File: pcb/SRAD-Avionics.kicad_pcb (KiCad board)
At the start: 4 copper layers, 75.8 x 82.9 mm, 48 parts, among them J1 Conn_01x02_Socket, J2 Conn_01x02_Socket, J3 USB_C_Receptacle_USB2.0_16P, SW1 SW_DIP_x01, U1 MS5607-02BA, U2 STM32H503RBTx, U3 MCP73831-2-MC, U4 TC2185-3.3VxCTTR, U5 USBLC6-2SC6, U6 TCAN332G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

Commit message: New dir structure. USB, CAN, power layout done. Started CubeIDE project
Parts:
- moved R4 38.6 mm to (146.3, 57.6)
- moved C2 38.3 mm to (138.3, 58.7), turned to -90 degrees
- moved C3 37.8 mm to (137.9, 66.3), turned to -90 degrees
- moved C8 36.1 mm to (157.5, 66.6), turned to 90 degrees
- moved D2 35.3 mm to (146.3, 60.7)
- moved U4 35.1 mm to (140.6, 66.6), turned to -90 degrees
- moved C4 35.1 mm to (140.5, 69.6)
- moved C9 34.0 mm to (167.9, 66.6), turned to 90 degrees
- moved R3 33.9 mm to (150.3, 57.6), turned to 180 degrees
- moved C5 33.3 mm to (143.3, 66.8), turned to 90 degrees
- moved C1 33.3 mm to (142.9, 58.7), turned to -90 degrees
- moved TP4 32.4 mm to (180.3, 62.9)
- moved R1 32.4 mm to (146.3, 63.7)
- moved C7 30.8 mm to (149.5, 80.9), turned to 180 degrees
- moved D1 30.7 mm to (150.3, 60.7)
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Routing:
- net +3.3V: track 17.0 -> 60.1 mm, vias 6 -> 17
- net GNDD: track 22.4 -> 60.9 mm, vias 12 -> 38
- net /FDCAN_TX: track 0.00 -> 33.6 mm, vias 0 -> 2
- net /FDCAN_RX: track 0.00 -> 31.7 mm, vias 0 -> 2
- net Net-(C6-Pad1): track 0.00 -> 28.7 mm, vias 0 -> 2
- net VDDA: track 0.00 -> 13.3 mm, vias 0 -> 3
- net /Battery Management/V_BAT: track 0.00 -> 13.2 mm, vias 0 -> 4
- net /Battery Management/STAT: track 0.00 -> 12.6 mm, vias 0 -> 2
- net /BOOT0: track 2.14 -> 11.7 mm
- net /Battery Management/V_USB: track 5.80 -> 12.7 mm, vias 3 -> 6
- net GNDA: track 0.00 -> 6.33 mm
- net Net-(U3-PROG): track 0.00 -> 6.32 mm
- net Net-(D2-K): track 0.00 -> 3.13 mm
- net Net-(D1-A): track 0.00 -> 3.12 mm
- net Net-(U4-BP): track 0.00 -> 1.88 mm
- added copper zone on In2.Cu, net +3.3V
- added copper zone on In2.Cu, net /Battery Management/V_BAT

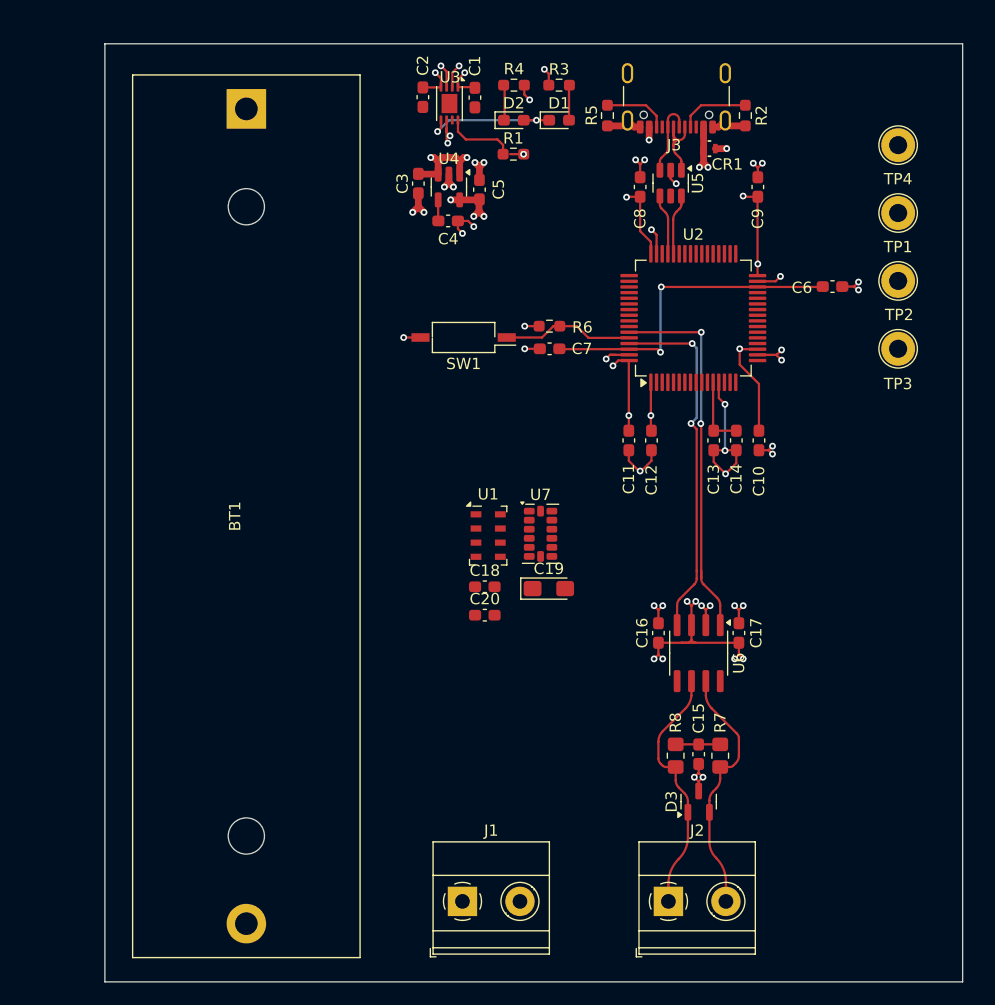
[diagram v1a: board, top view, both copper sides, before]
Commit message: Routed reset monitor, all test points, 128 MBit flash, sensors, analog-digital jumper switches
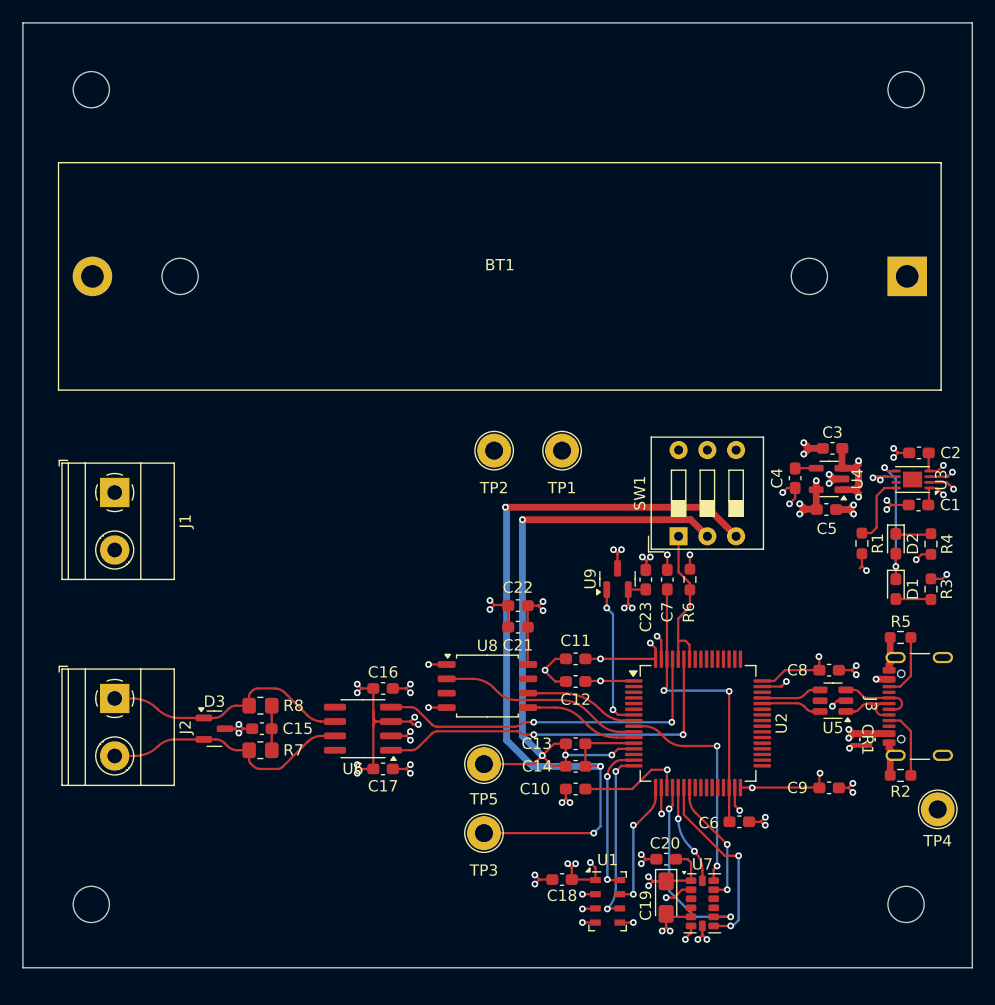
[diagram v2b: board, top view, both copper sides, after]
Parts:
- added C21: 100nF, Capacitor_SMD:C_0603_1608Metric_Pad1.08x0.95mm_HandSolder, F.Cu at (146.7, 105.5)
- added C22: 4.7uF, Capacitor_SMD:C_0603_1608Metric_Pad1.08x0.95mm_HandSolder, F.Cu at (146.7, 103.6)
- added C23: 100nF, Capacitor_SMD:C_0603_1608Metric_Pad1.08x0.95mm_HandSolder, F.Cu at (158.0, 101.3)
- added H1: MountingHole, MountingHole:MountingHole_3.2mm_M3, F.Cu at (109.0, 130.0)
- added H2: MountingHole, MountingHole:MountingHole_3.2mm_M3, F.Cu at (181.0, 130.0)
- added H3: MountingHole, MountingHole:MountingHole_3.2mm_M3, F.Cu at (109.0, 58.0)
- added H4: MountingHole, MountingHole:MountingHole_3.2mm_M3, F.Cu at (181.0, 58.0)
- added TP5: TestPoint, TestPoint:TestPoint_Loop_D2.60mm_Drill1.6mm_Beaded, F.Cu at (143.7, 117.6)
- added U8: W25Q128JVS, Package_SO:SOIC-8_5.23x5.23mm_P1.27mm, F.Cu at (144.0, 110.7)
- added U9: MCP130-xxxxTT, Package_TO_SOT_SMD:SOT-23, F.Cu at (155.5, 101.2)
- SW1: value SW_DIP_x01 -> SW_DIP_x03; footprint Button_Switch_SMD:SW_DIP_SPSTx01_Slide_Copal_CHS-01B_W7.62mm_P1.27mm -> Button_Switch_THT:SW_DIP_SPSTx03_Slide_9.78x9.8mm_W7.62mm_P2.54mm
- moved BT1 60.2 mm to (181.1, 74.5), turned to 180 degrees
- moved R2 59.9 mm to (180.5, 118.6), turned to 180 degrees
- moved J3 59.3 mm to (183.2, 112.5), turned to 90 degrees
- moved TP4 58.8 mm to (183.8, 121.6), turned to -90 degrees
- moved TP3 56.3 mm to (143.7, 123.7), turned to -90 degrees
- moved R3 55.3 mm to (183.2, 102.1), turned to 90 degrees
- moved R4 54.8 mm to (183.2, 98.2), turned to -90 degrees
- moved CR1 54.1 mm to (177.6, 115.4), turned to -90 degrees
- moved C2 53.9 mm to (182.1, 90.1), turned to 180 degrees
- moved C9 53.5 mm to (174.2, 119.7), turned to 0 degrees
- moved C1 53.2 mm to (182.1, 94.7), turned to 180 degrees
- moved R5 52.9 mm to (180.5, 106.4), turned to 180 degrees
- moved U3 52.7 mm to (181.6, 92.5), turned to 180 degrees
- moved J2 52.1 mm to (111.1, 111.8), turned to -90 degrees
- moved D1 51.0 mm to (180.1, 102.1), turned to -90 degrees
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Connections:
- C19 pad 1: Net-(U7-VDD_I/O) -> +3.3V
- C20 pad 1: Net-(U7-VDD_I/O) -> +3.3V
- J1 pad 1: unconnected-(J1-Pin_1-Pad1) -> +3.3V
- J1 pad 2: unconnected-(J1-Pin_2-Pad2) -> GNDD
- SW1 pad 2: +3.3V -> VDDA
- U1 pad 4: /Sensors/pres_cs -> GNDD
- U1 pad 5: /Sensors/pres_cs -> GNDD
- U1 pad 6: /Sensors/pres_miso -> /pres_miso
- U1 pad 7: /Sensors/pres_mosi -> /pres_mosi
- U1 pad 8: /Sensors/pres_sclk -> /pres_clk
- U2 pad 10: unconnected-(U2-PC2-Pad10) -> /flash_miso
- U2 pad 11: unconnected-(U2-PC3-Pad11) -> /flash_mosi
- U2 pad 15: unconnected-(U2-PA1-Pad15) -> /pres_clk
- U2 pad 16: unconnected-(U2-PA2-Pad16) -> /pres_miso
- U2 pad 17: unconnected-(U2-PA3-Pad17) -> /pres_mosi
- U2 pad 20: unconnected-(U2-PA4-Pad20) -> /accel_int1
- U2 pad 21: unconnected-(U2-PA5-Pad21) -> /accel_clk
- U2 pad 22: unconnected-(U2-PA6-Pad22) -> /accel_int2
- U2 pad 23: unconnected-(U2-PA7-Pad23) -> /accel_miso
- U2 pad 58: unconnected-(U2-PB6-Pad58) -> /BOOT0
- U2 pad 7: unconnected-(U2-NRST-Pad7) -> Net-(U2-NRST)
- U2 pad 8: unconnected-(U2-PC0-Pad8) -> /flash_clk
- U2 pad 9: unconnected-(U2-PC1-Pad9) -> /accel_mosi
- U7 pad 1: Net-(U7-VDD_I/O) -> +3.3V
- U7 pad 12: /Sensors/accel_miso -> /accel_miso
- U7 pad 13: /Sensors/accel_mosi -> /accel_mosi
- U7 pad 14: /Sensors/accel_sclk -> /accel_clk
- U7 pad 6: Net-(U7-VDD_I/O) -> +3.3V
- U7 pad 7: /Sensors/accel_cs -> GNDD
- U7 pad 8: /Sensors/accel_int1 -> /accel_int2
- U7 pad 9: /Sensors/accel_int2 -> /accel_int1
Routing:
- net GNDA: track 6.33 -> 74.9 mm, vias 0 -> 3
- net VDDA: track 13.3 -> 60.0 mm, vias 3 -> 4
- net GNDD: track 60.9 -> 98.4 mm, vias 38 -> 62
- net +3.3V: track 60.1 -> 85.3 mm, vias 17 -> 26
- net /accel_mosi: track 0.00 -> 19.9 mm, vias 0 -> 2
- net /flash_miso: track 0.00 -> 18.0 mm
- net /accel_int1: track 0.00 -> 17.1 mm, vias 0 -> 2
- net /accel_int2: track 0.00 -> 16.8 mm, vias 0 -> 2
- net /pres_miso: track 0.00 -> 15.4 mm, vias 0 -> 2
- net /pres_clk: track 0.00 -> 13.4 mm, vias 0 -> 2
- net Net-(U2-NRST): track 0.00 -> 12.9 mm, vias 0 -> 2
- net /accel_miso: track 0.00 -> 11.6 mm, vias 0 -> 2
- net /pres_mosi: track 0.00 -> 11.5 mm, vias 0 -> 2
- net /flash_mosi: track 0.00 -> 10.1 mm
- net /flash_clk: track 0.00 -> 9.99 mm
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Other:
- board size 75.8 x 82.9 mm -> 83.9 x 83.5 mm
- board text removed: "${REFERENCE}"
